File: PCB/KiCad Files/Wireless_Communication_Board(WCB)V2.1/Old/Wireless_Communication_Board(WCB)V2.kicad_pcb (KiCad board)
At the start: 4 copper layers, 52.5 x 38.3 mm, 44 parts, among them J1 USB_B_Micro, J2 Power In, J3 Conn_01x04, J4 Conn_01x04, J5 Conn_01x04, J6 Conn_01x04, J7 Conn_01x04, Q2 UMH3N, U1 ESP32-PICO-MINI-02, U2 CP2102N-A02-GQFN28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

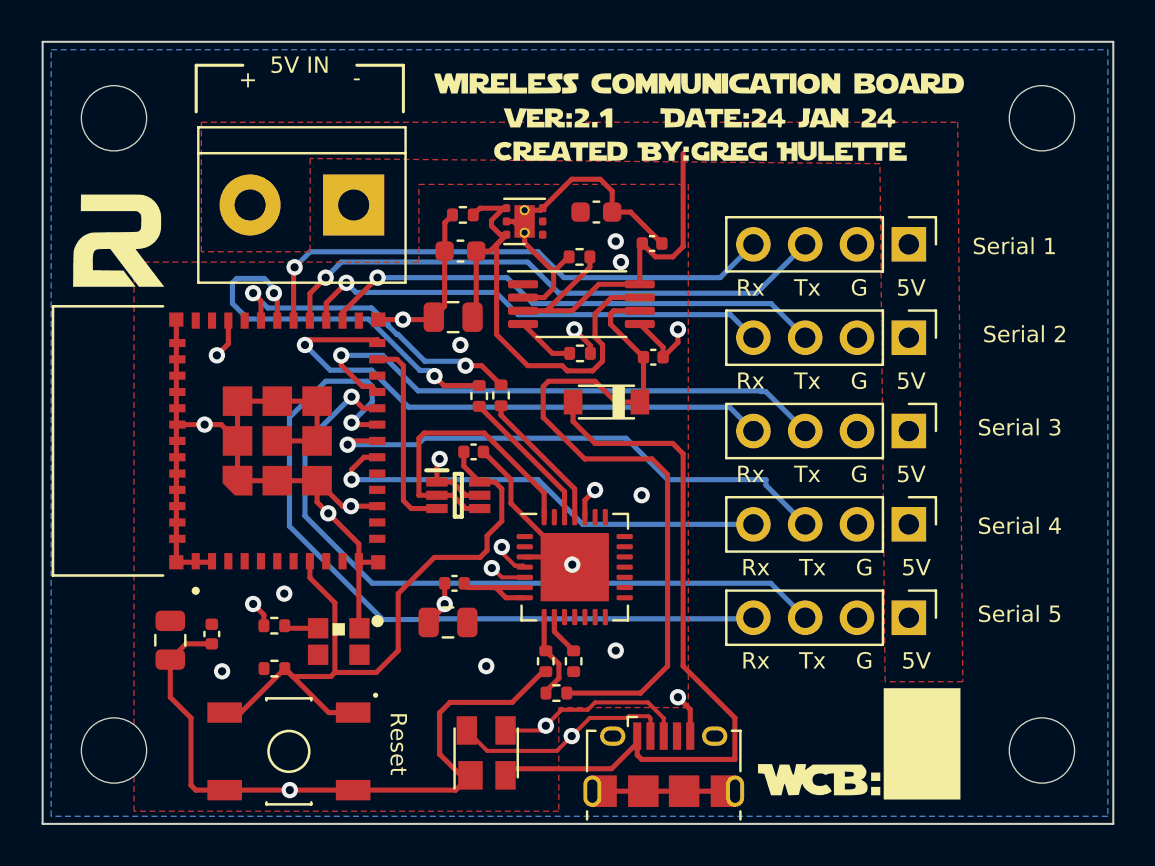
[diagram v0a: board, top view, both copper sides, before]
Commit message: Added WCB V2.2 and working on the code some.
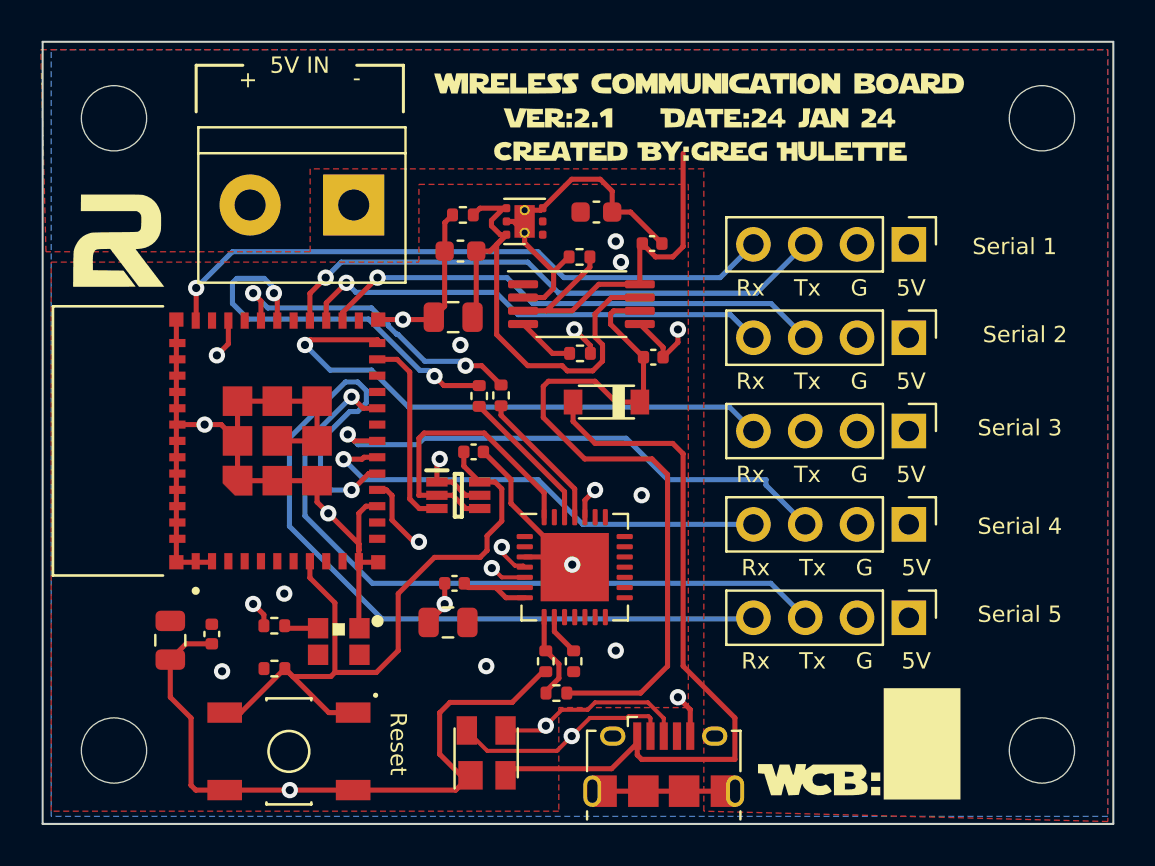
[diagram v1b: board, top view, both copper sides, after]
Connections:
- U1 pad 15: unconnected-(U1-Pad15) -> TX3
- U1 pad 16: unconnected-(U1-Pad16) -> RX5
- U1 pad 19: RX5 -> unconnected-(U1-Pad19)
- U1 pad 21: TX3 -> unconnected-(U1-Pad21)
- U1 pad 22: TX_HEADER -> unconnected-(U1-Pad22)
- U1 pad 29: RX1 -> unconnected-(U1-Pad29)
- U1 pad 35: unconnected-(U1-Pad35) -> RX1
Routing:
- net RX5: track 38.4 -> 42.9 mm
- net RX1: track 26.6 -> 30.9 mm
- net TX3: track 27.1 -> 25.0 mm
- net GND: track 122.6 -> 122.0 mm, vias 10 -> 9
